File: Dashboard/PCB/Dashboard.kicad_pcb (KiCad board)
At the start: 4 copper layers, 95.9 x 92.1 mm, 99 parts, among them J1 Display, J2 Conn_01x26_Female, J3 LED, J7 PROGRAMMER, P1 USB_C_Plug, Q1 Q_NMOS_GDS, SW1 SW_SPST, U1 STM32F767ZIT6, U10 24LC01, U3 MP2359DJ-LF-Z, U4 AS4C1M16S-6TCN, U5 AT25SF128A-SHB-T, U6 MP2332H, U7 MCP2561-E-SN, U8 MCP2561-E-SN, U9 ESP-12S, Y1 Crystal_GND24

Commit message: Add text to pcb
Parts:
- removed the G*** at (133.1, 71.1)
- added G***: LOGO, PGR_logo:calliper, B.Cu at (179.6, 117.2)
- added G***: LOGO, PGR_logo:logo, B.Cu at (144.9, 42.5)
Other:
- board text added: "Dashboard v1.0 Marcin Nadarzyński"

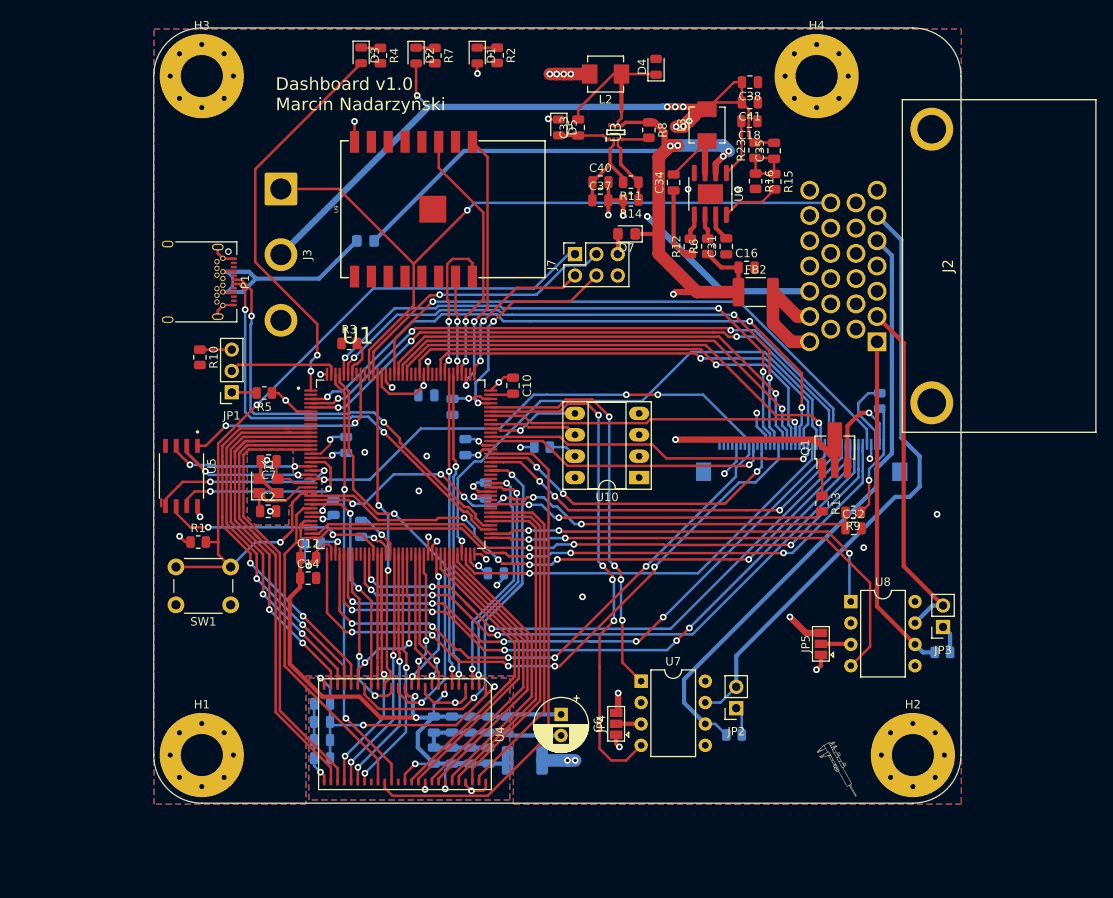
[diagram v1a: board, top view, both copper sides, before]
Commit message: Add new PCB for Dashboard (#34)
* Add usb C to board

* Add reset and pd pin to esp

* Switch footprints of converter

* Add LED Driver

* Add text to pcb

* New PCB for Dashboard
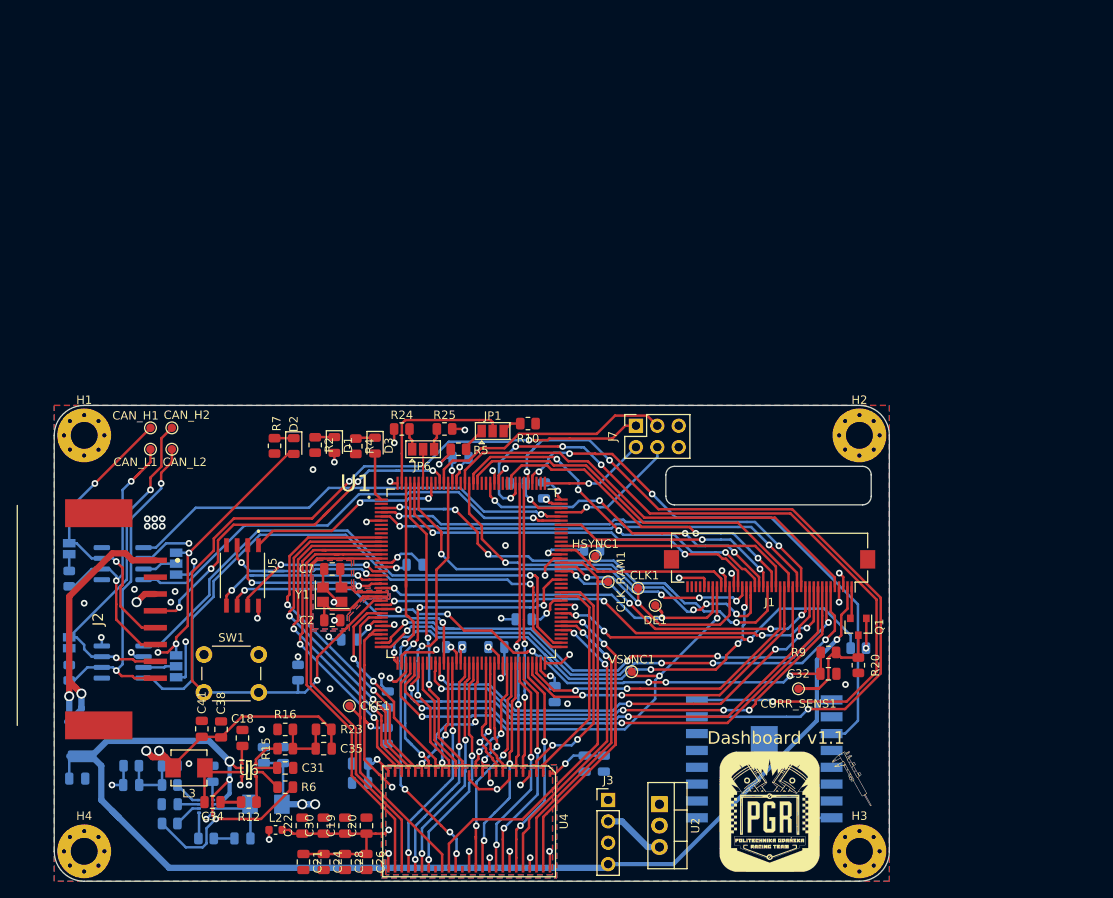
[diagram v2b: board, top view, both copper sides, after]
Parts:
- removed C4: 100nF, Capacitor_SMD:C_0805_2012Metric
- removed C6: 470uF, Capacitor_THT:CP_Radial_D6.3mm_P2.50mm
- removed D4: D_Schottky, Diode_SMD:D_0805_2012Metric
- removed D5: 1N4148, Diode_SMD:D_0805_2012Metric
- removed D6, D7: D_Schottky, Diode_SMD:D_0805_2012Metric_Pad1.15x1.40mm_HandSolder
- removed FB1: Ferrite_Bead, Capacitor_SMD:C_1812_4532Metric
- removed the G*** at (179.6, 117.2)
- removed the G*** at (144.9, 42.5)
- removed the G*** at (178.3, 117.2)
- removed P1: USB_C_Plug, Connector_USB:USB_C_Receptacle_Amphenol_12401548E4-2A
- removed R21: 10k, Resistor_SMD:R_0805_2012Metric
- removed U10: 24LC01, Package_DIP:DIP-8_W7.62mm_Socket_LongPads
- added C36: 1uF, Capacitor_SMD:C_0805_2012Metric, B.Cu at (99.1, 121.4)
- added C39: 10pF, Capacitor_SMD:C_0805_2012Metric, B.Cu at (94.5, 119.1)
- added C42: 22uF, Capacitor_SMD:C_0805_2012Metric, B.Cu at (110.2, 115.6)
- added CAN_H1: TestPoint, TestPoint:TestPoint_Pad_D1.0mm, F.Cu at (96.8, 76.7)
- added CAN_H2: TestPoint, TestPoint:TestPoint_Pad_D1.0mm, F.Cu at (99.3, 76.7)
- added CAN_L1: TestPoint, TestPoint:TestPoint_Pad_D1.0mm, F.Cu at (96.8, 79.2)
- added CAN_L2: TestPoint, TestPoint:TestPoint_Pad_D1.0mm, F.Cu at (99.3, 79.2)
- added CKE1: TestPoint, TestPoint:TestPoint_Pad_D1.0mm, F.Cu at (120.4, 109.7)
- added CLK1: TestPoint, TestPoint:TestPoint_Pad_D1.0mm, F.Cu at (154.7, 95.8)
- added CLK_RAM1: TestPoint, TestPoint:TestPoint_Pad_D1.0mm, F.Cu at (151.1, 95.0)
- added CURR_SENS1: TestPoint, TestPoint:TestPoint_Pad_D1.0mm, F.Cu at (173.7, 107.7)
- added DE1: TestPoint, TestPoint:TestPoint_Pad_D1.0mm, F.Cu at (156.7, 97.8)
- added G***: LOGO, PGR_logo:logo_16x16mm, F.Cu at (170.3, 122.3)
- added G***: LOGO, PGR_logo:calliper, F.Cu at (180.1, 118.4)
- added HSYNC1: TestPoint, TestPoint:TestPoint_Pad_D1.0mm, F.Cu at (149.6, 91.9)
- added JP6: BOOT0, Jumper:SolderJumper-3_P1.3mm_Open_Pad1.0x1.5mm, F.Cu at (129.2, 79.2)
- added L1: 3.3uH, Inductor_SMD:L_Vishay_IHLP-1616, B.Cu at (110.5, 121.4)
- added R24: 10k, Resistor_SMD:R_0805_2012Metric, F.Cu at (126.6, 76.8)
- added R25: 10k, Resistor_SMD:R_0805_2012Metric, F.Cu at (131.7, 76.8)
- added R26: 40.2k, Resistor_SMD:R_0805_2012Metric, B.Cu at (94.5, 116.8)
- added U2: IFX27001TFV33, Package_TO_SOT_THT:TO-220-3_Vertical, F.Cu at (157.2, 121.4)
- added VSYNC1: TestPoint, TestPoint:TestPoint_Pad_D1.0mm, F.Cu at (153.9, 105.7)
- C10, C12, C14, C16, FB2, JP4, JP5, R1, R13, U9: moved to B.Cu
- C19, C20, C21, C22, C24, C26, C28, C30, J1, R20: moved to F.Cu
- C33: value 10nF -> 1uF; moved to B.Cu
- C37: value 10uF -> 1uF; moved to B.Cu
- C40: value 10uF -> 22uF; moved to B.Cu
- H1, H2, H3, H4: footprint MountingHole:MountingHole_5mm_Pad_Via -> MountingHole:MountingHole_3.2mm_M3_Pad_Via
- J2: value Conn_01x26_Female -> 34912-6080; footprint Konektor:64734231 -> DashboardConnector:349126080
- J3: value LED -> Conn_01x04_Female; footprint Connector_Wire:SolderWire-2sqmm_1x03_P7.8mm_D2mm_OD3.9mm -> Connector_PinHeader_2.54mm:PinHeader_1x04_P2.54mm_Vertical
- JP1: footprint Connector_PinSocket_2.54mm:PinSocket_1x03_P2.54mm_Vertical -> Jumper:SolderJumper-3_P1.3mm_Open_Pad1.0x1.5mm
- JP2, JP3: footprint Connector_PinSocket_2.54mm:PinSocket_1x02_P2.54mm_Vertical -> Jumper:SolderJumper-2_P1.3mm_Open_Pad1.0x1.5mm; moved to B.Cu
- L2: value 10uH -> 39nH; footprint Inductor_SMD:L_Vishay_IHLP-1616 -> Inductor_SMD:L_0603_1608Metric
- Q1: footprint Package_TO_SOT_SMD:SOT-89-3_Handsoldering -> Package_TO_SOT_SMD:SOT-23
- R11: value R -> 20k; moved to B.Cu
- R14: value R -> 13k; moved to B.Cu
- R3: value 10k -> 100k; moved to B.Cu
- R8: value 100k -> R; moved to B.Cu
- U3: value MP2359DJ-LF-Z -> MP2332H; moved to B.Cu
- U6: footprint Package_SO:SOIC-8-1EP_3.9x4.9mm_P1.27mm_EP2.29x3mm -> SOT-583:SOTFL50P160X60-8N
- U7, U8: footprint Package_DIP:DIP-8_W7.62mm -> Package_SO:SOIC-8_3.9x4.9mm_P1.27mm; moved to B.Cu
- moved H4 126.7 mm to (88.9, 127.0)
- moved H3 120.7 mm to (181.0, 127.0)
- moved JP3 103.8 mm to (87.1, 102.2), turned to 90 degrees
- moved R18 103.7 mm to (87.1, 105.8), turned to 270 degrees
- moved C16 100.0 mm to (88.1, 118.4)
- moved C38 99.3 mm to (105.2, 112.5), turned to 270 degrees
- moved R8 99.2 mm to (103.4, 125.5), turned to 180 degrees
- moved C41 98.8 mm to (102.9, 112.5), turned to 270 degrees
- moved J2 98.2 mm to (90.6, 99.4), turned to 270 degrees
- moved L3 98.1 mm to (101.3, 117.1), turned to 180 degrees
- moved L2 98.0 mm to (111.6, 124.5), turned to 0 degrees
- moved FB2 96.0 mm to (88.6, 113.7), turned to 90 degrees
- moved C18 94.8 mm to (107.7, 113.5), turned to 270 degrees
- moved U3 93.7 mm to (103.4, 121.7), turned to 180 degrees
- moved C34 91.7 mm to (104.1, 121.2), turned to 180 degrees
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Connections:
- C33 pad 1: Net-(C33-Pad1) -> GND
- C37 pad 1: GND -> Net-(C37-Pad1)
- C37 pad 2: +3V3 -> Net-(C37-Pad2)
- J1 pad 2: DISPLAY_LED+ -> +12L
- J1 pad 31: /DISPLAY_EN -> +3V3
- J2 pad 1: CAN_L2 -> +12V
- J2 pad 2: CAN_H2 -> GND
- J2 pad 3: Net-(J2-Pad3) -> +5V
- J2 pad 4: Net-(J2-Pad4) -> LED_DATA
- J2 pad 5: CAN_L1 -> CAN_H1
- J2 pad 6: CAN_H1 -> CAN_L1
- J2 pad 7: Net-(J2-Pad7) -> CAN_H2
- J2 pad 8: Net-(J2-Pad8) -> CAN_L2
- J3 pad 1: LED_DATA -> GND
- L2 pad 1: Net-(C33-Pad2) -> +3V3
- L2 pad 2: +3V3 -> +3.3VA
- Q1 pad 2: +12L -> DISPLAY_LED-
- Q1 pad 3: DISPLAY_LED+ -> Net-(CURR_SENS1-Pad1)
- R11 pad 1: Net-(R11-Pad1) -> Net-(C39-Pad1)
- R11 pad 2: GND -> Net-(R11-Pad2)
- R14 pad 1: Net-(R11-Pad1) -> Net-(C39-Pad1)
- R14 pad 2: +3V3 -> GND
- R16 pad 2: Net-(R16-Pad2) -> GND
- R20 pad 1: DISPLAY_LED- -> Net-(CURR_SENS1-Pad1)
- R3 pad 1: GND -> +12L
- R8 pad 1: +12L -> Net-(C37-Pad1)
- R9 pad 1: DISPLAY_LED- -> Net-(CURR_SENS1-Pad1)
- U1 pad 138: Net-(R3-Pad2) -> Net-(JP6-Pad2)
- U3 pad 1: Net-(C33-Pad1) -> Net-(C33-Pad2)
- U3 pad 2: GND -> +12L
- U3 pad 3: Net-(R11-Pad1) -> Net-(C37-Pad2)
- U3 pad 4: Net-(R8-Pad2) -> GND
- U3 pad 5: +12L -> Net-(R8-Pad2)
- U3 pad 6: Net-(C33-Pad2) -> Net-(R3-Pad2)
- U3 pad 7: (no net) -> Net-(C36-Pad2)
- U3 pad 8: (no net) -> Net-(R11-Pad2)
- U9 pad 1: ESP_RESET -> Net-(U9-Pad1)
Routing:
- net ESP_UART_RX: track 11.7 -> 86.8 mm, vias 2 -> 3
- net ESP_UART_TX: track 18.4 -> 91.9 mm, vias 2 -> 5
- net USB_OTG_DP: track 51.8 -> 0.00 mm, vias 2 -> 0
- net USB_OTG_DM: track 51.5 -> 0.00 mm, vias 2 -> 0
- net GND: track 129.1 -> 77.6 mm, vias 27 -> 49
- net +5V: track 216.5 -> 167.5 mm, vias 10 -> 6
- net LED_DATA: track 87.3 -> 44.7 mm, vias 1 -> 4
- net SIGNAL_LED: track 47.5 -> 5.78 mm, vias 2 -> 0
- net +12L: track 136.2 -> 177.8 mm, vias 6 -> 4
- net CAN_H1: track 72.5 -> 35.1 mm, vias 0 -> 2
- net CAN_L1: track 72.4 -> 35.8 mm, vias 0 -> 2
- net ESP_EN: track 30.9 -> 66.0 mm, vias 2 -> 3
- net ESP_RESET: track 32.1 -> 0.00 mm, vias 2 -> 0
- net Net-(D6-Pad2): track 29.4 -> 0.00 mm
- net +3.3VA: track 91.8 -> 63.8 mm, vias 5 -> 6
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- added copper zone on In1.Cu, net +3.3VA
- added copper zone on In1.Cu, net +3V3
- added copper zone on In2.Cu, net GND
- removed copper zone on In2.Cu, net +3V3
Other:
- board size 95.9 x 92.1 mm -> 99.2 x 56.5 mm
- board text added: "Dashboard v1.1"
- board text added: "M. NADARZYŃSKI"
- board text removed: "Dashboard v1.0 Marcin Nadarzyński"
- board text removed: "M. NADARZYNSKI"
